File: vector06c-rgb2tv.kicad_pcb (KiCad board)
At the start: 2 copper layers, 95.9 x 30.1 mm, 77 parts, among them J1 Conn_01x09, Q1 4.43, U1 CXA2075M, U2 7400, U3 7474, U4 74HC240

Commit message: rename project files, fix Improver's nick
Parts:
- TP1, TP10, TP11, TP12, TP13, TP14, TP15, TP16, TP17, TP18, TP19, TP2, TP3, TP4, TP5, TP6, TP7, TP8, TP9: footprint improve-rgb2tv:PAD-150-60 -> vector06c-rgb2tv:PAD-150-60
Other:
- board text added: "Vector-06C video mod Design by Improver This custom board by desaster https://zx-pk.ru/threads/8739-vektor-06ts-videovykhod-podklyuchenie-k-tv/"
- board text removed: "Vector-06C video mod Design by Improve This custom board by desaster https://zx-pk.ru/threads/8739-vektor-06ts-videovykhod-podklyuchenie-k-tv/"
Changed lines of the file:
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@@
   )
   (setup
-    (last_trace_width 0.762)
+    (last_trace_width 0.2032)
     (user_trace_width 0.254)
     (user_trace_width 0.508)
@@
     (add_net "Net-(U3-Pad8)")
   )
-  (module improve-rgb2tv:PAD-150-60 (layer F.Cu)
+  (module vector06c-rgb2tv:PAD-150-60 (layer F.Cu)
     (at 99.568 97.155)
     (fp_text reference TP3 (at 0 2) (layer F.SilkS) hide
@@
     )
   )
-  (module improve-rgb2tv:PAD-150-60 (layer F.Cu)
+  (module vector06c-rgb2tv:PAD-150-60 (layer F.Cu)
     (at 105.918 121.92)
     (fp_text reference TP1 (at 0 2) (layer F.SilkS) hide
@@
       (net 36 "Net-(TP1-Pad1)"))
   )
-  (module improve-rgb2tv:PAD-150-60 (layer F.Cu)
+  (module vector06c-rgb2tv:PAD-150-60 (layer F.Cu)
     (at 102.743 121.92)
     (fp_text reference TP2 (at 0 2) (layer F.SilkS) hide
@@
       (net 37 "Net-(TP2-Pad1)"))
   )
-  (module improve-rgb2tv:PAD-150-60 (layer F.Cu)
+  (module vector06c-rgb2tv:PAD-150-60 (layer F.Cu)
     (at 102.743 97.155)
     (fp_text reference TP4 (at 0 2) (layer F.SilkS) hide
@@
       (net 39 "Net-(TP4-Pad1)"))
   )
-  (module improve-rgb2tv:PAD-150-60 (layer F.Cu)
+  (module vector06c-rgb2tv:PAD-150-60 (layer F.Cu)
     (at 99.568 121.92)
     (fp_text reference TP5 (at 0 2) (layer F.SilkS) hide
@@
       (net 40 "Net-(TP5-Pad1)"))
   )
-  (module improve-rgb2tv:PAD-150-60 (layer F.Cu)
+  (module vector06c-rgb2tv:PAD-150-60 (layer F.Cu)
     (at 154.94 121.285)
     (fp_text reference TP6 (at 0 2) (layer F.SilkS) hide
@@
       (net 41 "Net-(TP6-Pad1)"))
   )
-  (module improve-rgb2tv:PAD-150-60 (layer F.Cu)
+  (module vector06c-rgb2tv:PAD-150-60 (layer F.Cu)
     (at 189.865 104.14)
     (fp_text reference TP7 (at 0 2) (layer F.SilkS) hide
@@
     )
   )
-  (module improve-rgb2tv:PAD-150-60 (layer F.Cu)
+  (module vector06c-rgb2tv:PAD-150-60 (layer F.Cu)
     (at 154.94 96.52)
     (fp_text reference TP8 (at 0 2) (layer F.SilkS) hide
@@
       (net 7 +5V))
   )
-  (module improve-rgb2tv:PAD-150-60 (layer F.Cu)
+  (module vector06c-rgb2tv:PAD-150-60 (layer F.Cu)
     (at 105.918 97.155)
     (fp_text reference TP9 (at 0 2) (layer F.SilkS) hide
@@
       (net 56 GND))
   )
-  (module improve-rgb2tv:PAD-150-60 (layer F.Cu)
+  (module vector06c-rgb2tv:PAD-150-60 (layer F.Cu)
     (at 174.625 121.285 270)
     (fp_text reference TP10 (at 0 2 90) (layer F.SilkS) hide
@@
     )
   )
-  (module improve-rgb2tv:PAD-150-60 (layer F.Cu)
+  (module vector06c-rgb2tv:PAD-150-60 (layer F.Cu)
     (at 188.595 96.52 180)
     (fp_text reference TP11 (at 0 2) (layer F.SilkS) hide
@@
       (net 65 "Net-(C19-Pad2)"))
   )
-  (module improve-rgb2tv:PAD-150-60 (layer F.Cu)
+  (module vector06c-rgb2tv:PAD-150-60 (layer F.Cu)
     (at 183.515 96.52 180)
     (fp_text reference TP12 (at 0 2) (layer F.SilkS) hide
@@
       (net 67 "Net-(C21-Pad2)"))
   )
-  (module improve-rgb2tv:PAD-150-60 (layer F.Cu)
+  (module vector06c-rgb2tv:PAD-150-60 (layer F.Cu)
     (at 178.435 96.52 180)
     (fp_text reference TP13 (at 0 2) (layer F.SilkS) hide
@@
       (net 68 "Net-(C22-Pad2)"))
   )
-  (module improve-rgb2tv:PAD-150-60 (layer F.Cu)
+  (module vector06c-rgb2tv:PAD-150-60 (layer F.Cu)
     (at 189.865 109.22 90)
     (fp_text reference TP14 (at 0 2 90) (layer F.SilkS) hide
@@
       (net 58 "Net-(C7-Pad2)"))
   )
-  (module improve-rgb2tv:PAD-150-60 (layer F.Cu)
+  (module vector06c-rgb2tv:PAD-150-60 (layer F.Cu)
     (at 189.865 114.3 90)
     (fp_text reference TP15 (at 0 2 90) (layer F.SilkS) hide
@@
       (net 61 "Net-(C8-Pad2)"))
   )
-  (module improve-rgb2tv:PAD-150-60 (layer F.Cu)
+  (module vector06c-rgb2tv:PAD-150-60 (layer F.Cu)
     (at 178.435 121.285)
     (fp_text reference TP16 (at 0 2) (layer F.SilkS) hide
@@
       (net 56 GND))
   )
-  (module improve-rgb2tv:PAD-150-60 (layer F.Cu)
+  (module vector06c-rgb2tv:PAD-150-60 (layer F.Cu)
     (at 189.865 121.285)
     (fp_text reference TP17 (at 0 2) (layer F.SilkS) hide
@@
       (net 56 GND))
   )
-  (module improve-rgb2tv:PAD-150-60 (layer F.Cu)
+  (module vector06c-rgb2tv:PAD-150-60 (layer F.Cu)
     (at 182.245 121.285)
     (fp_text reference TP18 (at 0 2) (layer F.SilkS) hide
@@
       (net 56 GND))
   )
-  (module improve-rgb2tv:PAD-150-60 (layer F.Cu)
+  (module vector06c-rgb2tv:PAD-150-60 (layer F.Cu)
     (at 186.055 121.285)
     (fp_text reference TP19 (at 0 2) (layer F.SilkS) hide
@@
   (gr_arc (start 190.627 122.682) (end 190.627 124.46) (angle -90) (layer Edge.Cuts) (width 0.05))
   (gr_arc (start 98.298 122.682) (end 96.52 122.682) (angle -90) (layer Edge.Cuts) (width 0.05))
-  (gr_text "Vector-06C video mod\nDesign by Improve\nThis custom board by desaster\nhttps://zx-pk.ru/threads/8739-vektor-06ts-videovykhod-podklyuchenie-k-tv/" (at 186.436 115.824) (layer B.SilkS)
+  (gr_text "Vector-06C video mod\nDesign by Improver\nThis custom board by desaster\nhttps://zx-pk.ru/threads/8739-vektor-06ts-videovykhod-podklyuchenie-k-tv/" (at 186.436 115.824) (layer B.SilkS)
     (effects (font (size 0.75 0.75) (thickness 0.12)) (justify left mirror))
   )
-  (via (at 118.872 110.744) (size 0.8) (drill 0.4) (layers F.Cu B.Cu) (net 56))
   (segment (start 142.959999 96.308001) (end 142.24 97.028) (width 0.2032) (layer F.Cu) (net 1))
   (segment (start 143.51 95.758) (end 142.959999 96.308001) (width 0.2032) (layer F.Cu) (net 1))
@@
   (segment (start 102.362 109.9185) (end 101.6 109.9185) (width 0.254) (layer F.Cu) (net 51))
   (segment (start 104.013 102.3) (end 102.743 102.3) (width 0.254) (layer F.Cu) (net 52))
+  (via (at 118.872 110.744) (size 0.8) (drill 0.4) (layers F.Cu B.Cu) (net 56))
   (segment (start 106.855 116.473) (end 106.553 116.775) (width 0.762) (layer F.Cu) (net 56))
   (segment (start 108.458 116.473) (end 106.855 116.473) (width 0.762) (layer F.Cu) (net 56))

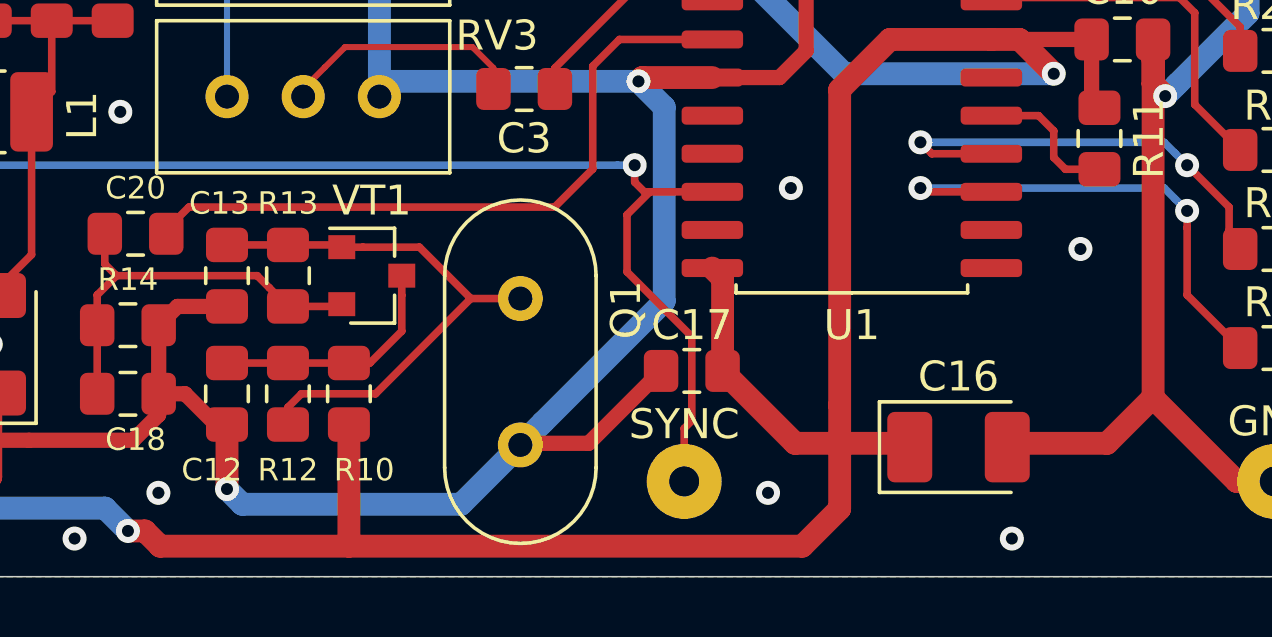
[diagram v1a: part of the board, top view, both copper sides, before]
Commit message: fix silkscreen layout
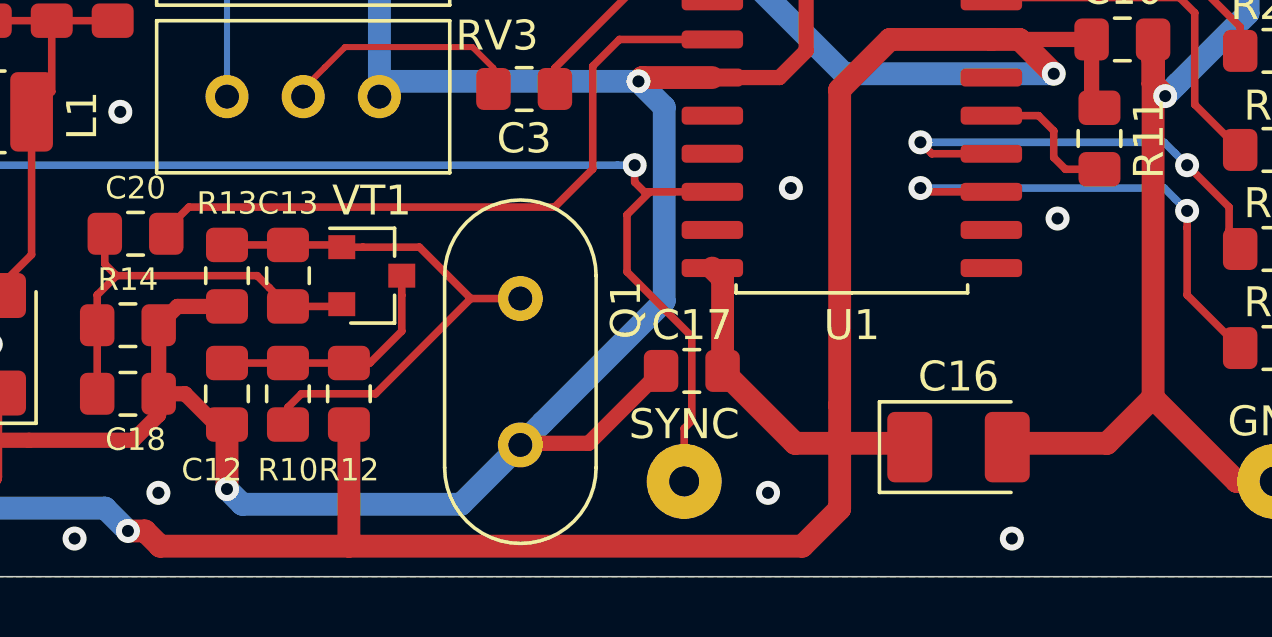
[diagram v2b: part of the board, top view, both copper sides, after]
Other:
- board text added: "Vector-06C RGB2TV Design by Improver https://zx-pk.ru/threads/8739-vektor-06ts-videovykhod-podklyuchenie-k-tv/ This custom board by desaster https://github.com/desaster/vector06c-rgb2tv/"
- board text added: "why is there two 0.1 side by side is one meant to go elsewhere?"
- board text removed: "Vector-06C video mod Design by Improver This custom board by desaster https://zx-pk.ru/threads/8739-vektor-06ts-videovykhod-podklyuchenie-k-tv/"
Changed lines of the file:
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@@
   (general
     (thickness 1.6)
-    (drawings 9)
+    (drawings 10)
     (tracks 573)
     (zones 0)
@@
     (tags "capacitor handsolder")
     (attr smd)
-    (fp_text reference C13 (at 2.413 -2.286 180) (layer F.SilkS)
+    (fp_text reference C13 (at 2.413 0 180) (layer F.SilkS)
       (effects (font (size 0.75 0.75) (thickness 0.12)))
     )
@@
     (tags "resistor handsolder")
     (attr smd)
-    (fp_text reference R10 (at 2.54 -2.54 180) (layer F.SilkS)
+    (fp_text reference R10 (at 2.54 0 180) (layer F.SilkS)
       (effects (font (size 0.75 0.75) (thickness 0.12)))
     )
@@
     (tags "resistor handsolder")
     (attr smd)
-    (fp_text reference R12 (at -2.54 -2.032 180) (layer F.SilkS)
+    (fp_text reference R12 (at -2.54 0 180) (layer F.SilkS)
       (effects (font (size 0.75 0.75) (thickness 0.12)))
     )
@@
     (tags "resistor handsolder")
     (attr smd)
-    (fp_text reference R13 (at -2.413 -2.032 180) (layer F.SilkS)
+    (fp_text reference R13 (at -2.413 0 180) (layer F.SilkS)
       (effects (font (size 0.75 0.75) (thickness 0.12)))
     )
@@
     )
   )
+  (gr_text "why is there two 0.1 side by side\nis one meant to go elsewhere?" (at 163.322 90.424) (layer Cmts.User)
+    (effects (font (size 1 1) (thickness 0.2)))
+  )
   (gr_line (start 190.627 124.46) (end 98.298 124.46) (layer Edge.Cuts) (width 0.05))
   (gr_line (start 192.405 96.139) (end 192.405 122.682) (layer Edge.Cuts) (width 0.05))
@@
   (gr_arc (start 190.627 122.682) (end 190.627 124.46) (angle -90) (layer Edge.Cuts) (width 0.05))
   (gr_arc (start 98.298 122.682) (end 96.52 122.682) (angle -90) (layer Edge.Cuts) (width 0.05))
-  (gr_text "Vector-06C video mod\nDesign by Improver\nThis custom board by desaster\nhttps://zx-pk.ru/threads/8739-vektor-06ts-videovykhod-podklyuchenie-k-tv/" (at 186.436 115.824) (layer B.SilkS)
+  (gr_text "Vector-06C RGB2TV\nDesign by Improver\nhttps://zx-pk.ru/threads/8739-vektor-06ts-videovykhod-podklyuchenie-k-tv/\nThis custom board by desaster\nhttps://github.com/desaster/vector06c-rgb2tv/" (at 186.944 113.538) (layer B.SilkS)
     (effects (font (size 0.75 0.75) (thickness 0.12)) (justify left mirror))
   )
@@
   (via (at 179.832 100.076) (size 0.8) (drill 0.4) (layers F.Cu B.Cu) (net 56))
   (via (at 183.896 100.33) (size 0.8) (drill 0.4) (layers F.Cu B.Cu) (net 56))
-  (via (at 168.148 113.538) (size 0.8) (drill 0.4) (layers F.Cu B.Cu) (net 56))
+  (via (at 167.386 112.522) (size 0.8) (drill 0.4) (layers F.Cu B.Cu) (net 56))
   (via (at 165.862 123.19) (size 0.8) (drill 0.4) (layers F.Cu B.Cu) (net 56))
   (via (at 134.62 123.19) (size 0.8) (drill 0.4) (layers F.Cu B.Cu) (net 56))

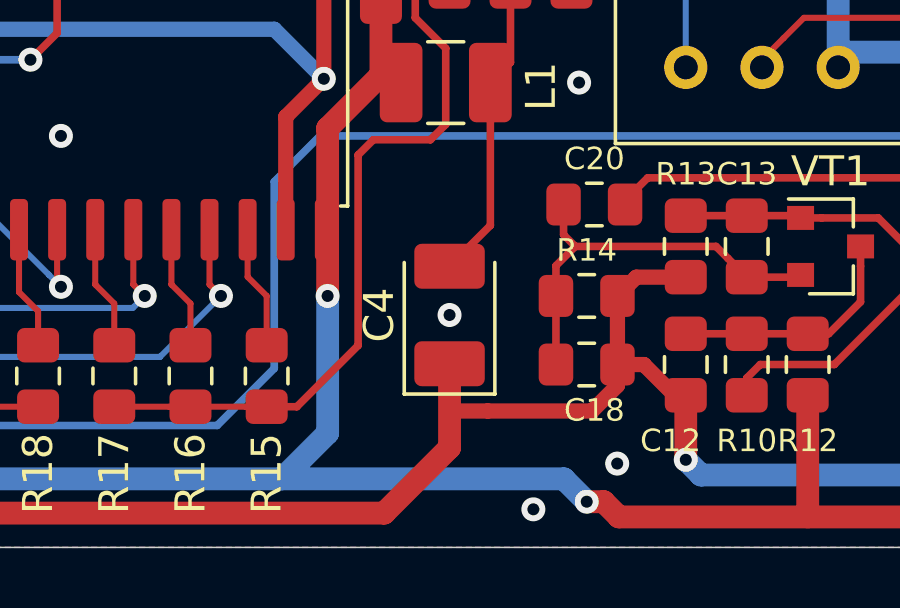
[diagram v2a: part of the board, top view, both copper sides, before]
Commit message: fix C4 orientation
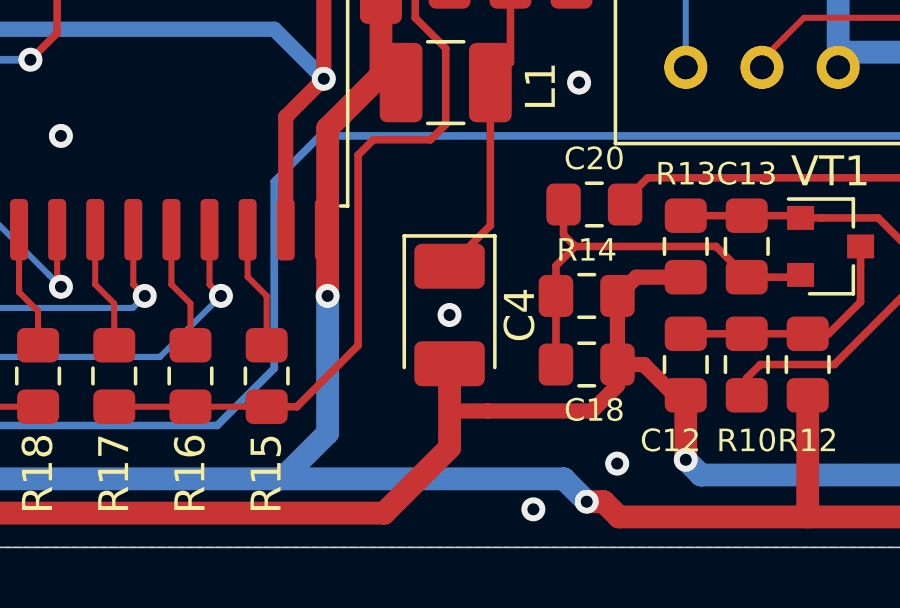
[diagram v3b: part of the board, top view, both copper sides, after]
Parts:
- turned C4 to 270 degrees
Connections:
- C4 pad 1: GND -> Net-(C4-Pad1)
- C4 pad 2: Net-(C4-Pad2) -> GND
- L1 pad 1: Net-(C4-Pad2) -> Net-(C4-Pad1)
- R1 pad 2: Net-(C4-Pad2) -> Net-(C4-Pad1)
- R2 pad 2: Net-(C4-Pad2) -> Net-(C4-Pad1)
- R3 pad 2: Net-(C4-Pad2) -> Net-(C4-Pad1)
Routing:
- net Net-(C4-Pad2): track 14.1 -> 0.00 mm
- net Net-(C4-Pad1): track 0.00 -> 14.1 mm
